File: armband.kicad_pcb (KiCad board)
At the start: 6 copper layers, 50 x 50 mm, 164 parts, among them IC1 STM32MP157AAB3, IC2 MT41K256M16TW-107_P, IC6 STPMIC1BPQR, IC7 S40FC004C1B2C00000, IC9 NXS0506UPZ, J4 Conn_01x03, SW1 SW_MEC_5G, SW2 SW_MEC_5G, U2 IS25LP064A-JLLE

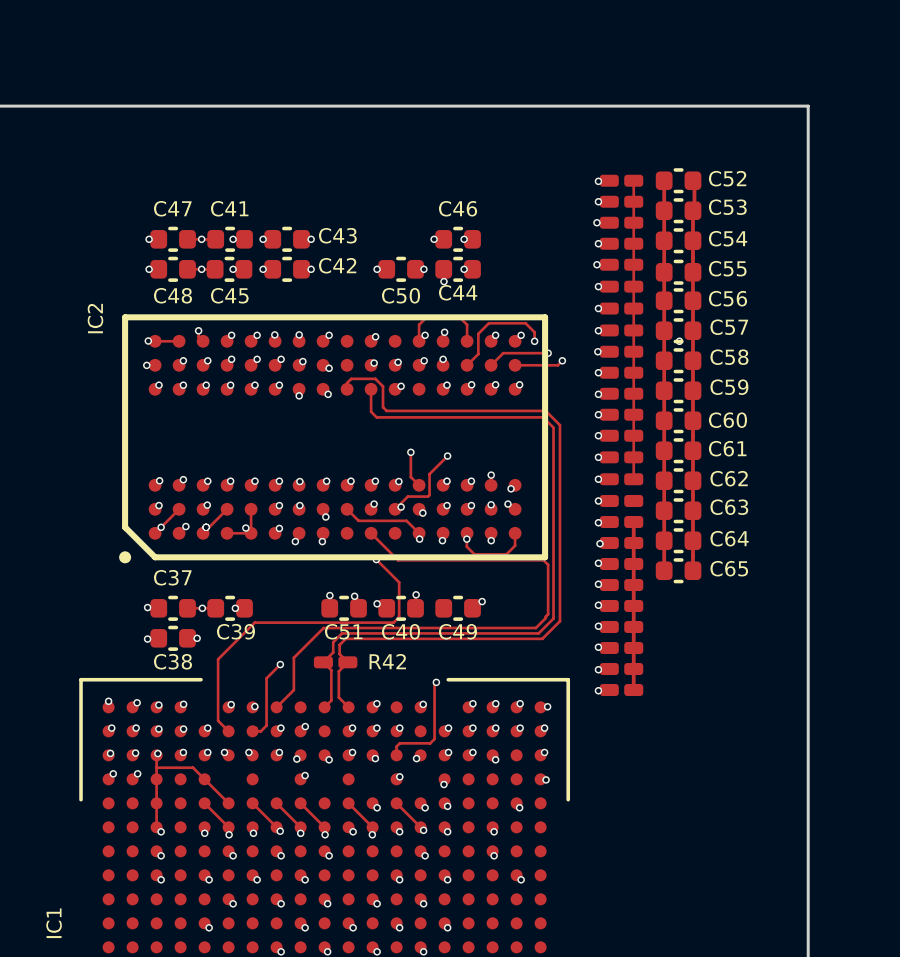
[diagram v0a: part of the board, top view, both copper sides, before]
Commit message: Add termination resistor conenctions + via for DQ
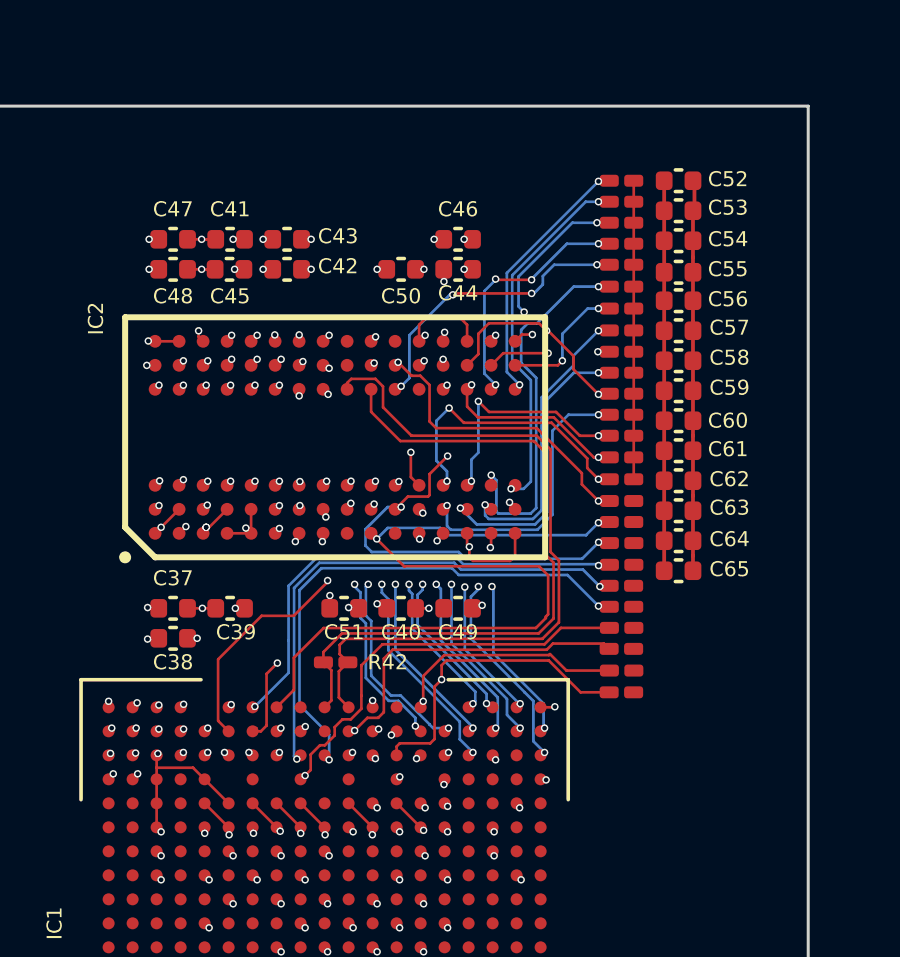
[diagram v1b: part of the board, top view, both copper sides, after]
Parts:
- moved R43 4.17 mm to (191.9, 76.7)
- moved R49 3.55 mm to (191.9, 80.2)
- moved R50 1.43 mm to (191.9, 77.3)
- moved R48 1.40 mm to (191.9, 75.9)
- moved R44 0.78 mm to (191.9, 80.9)
- moved R46 0.73 mm to (191.9, 79.5)
- moved R45 0.67 mm to (191.9, 78.8)
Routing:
- net DDR_CASN: track 24.7 -> 41.9 mm
- net DDR_WEN: track 23.2 -> 40.1 mm
- net DDR_BA0: track 18.5 -> 34.1 mm
- net DDR_BA2: track 24.1 -> 37.5 mm, vias 3 -> 2
- net DDR_A9: track 20.2 -> 32.2 mm
- net DDR_A13: track 19.1 -> 30.9 mm
- net DDR_RASN: track 24.2 -> 35.0 mm, vias 3 -> 2
- net DDR_CSN: track 22.4 -> 32.9 mm
- net DDR_A7: track 19.5 -> 29.0 mm
- net DDR_A0: track 20.5 -> 29.7 mm, vias 3 -> 4
- net DDR_A5: track 23.3 -> 32.5 mm
- net DDR_A3: track 20.3 -> 29.3 mm
- net DDR_A10: track 20.7 -> 29.6 mm, vias 3 -> 5
- net DDR_A14: track 17.2 -> 25.7 mm
- net DDR_A12: track 22.4 -> 30.7 mm, vias 3 -> 4
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
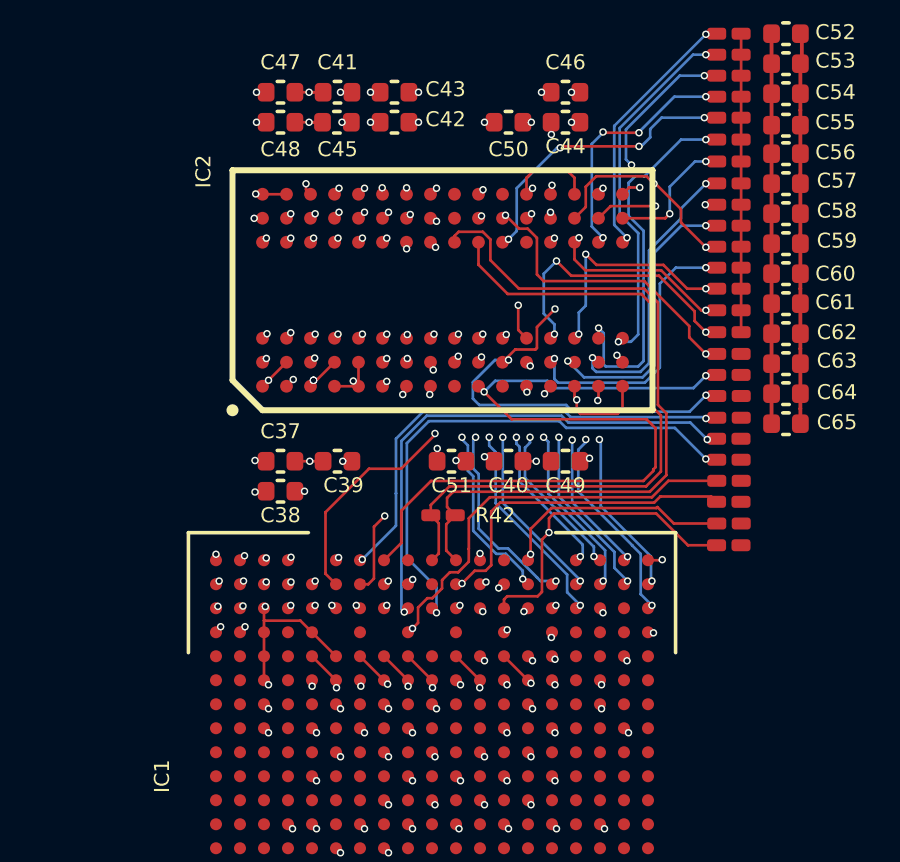
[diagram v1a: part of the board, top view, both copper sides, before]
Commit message: routed datalines - gl lengthmatching that!
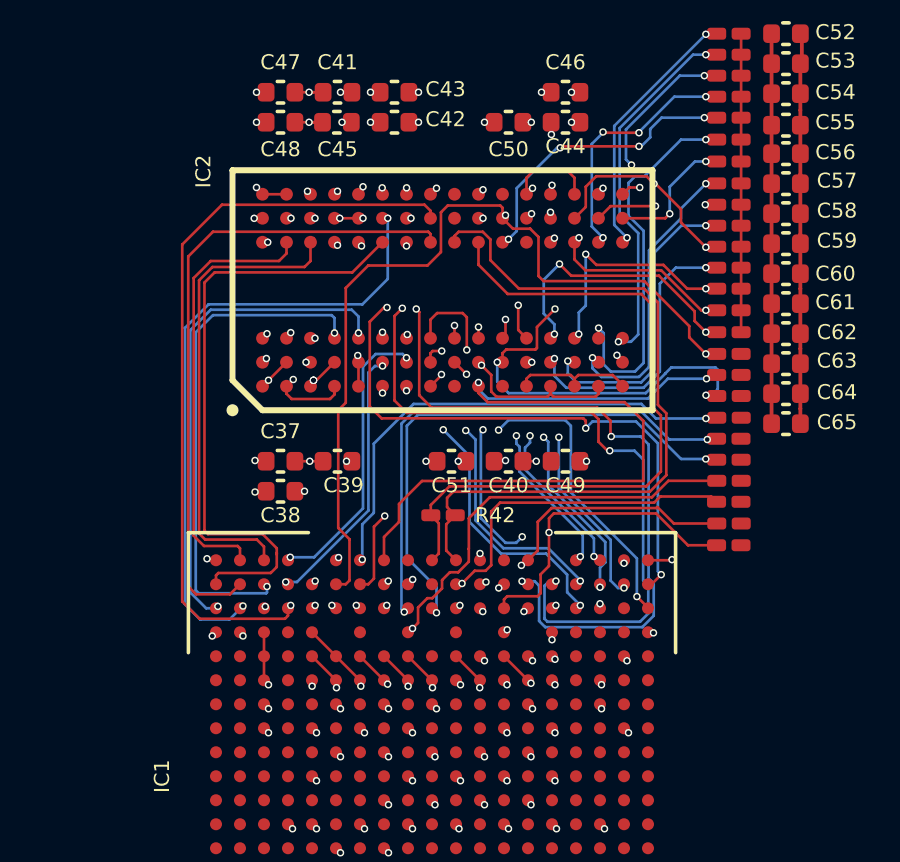
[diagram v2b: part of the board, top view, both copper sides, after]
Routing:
- net DDR_DQ5: track 0.37 -> 25.3 mm, vias 2 -> 1
- net DDR_DQ10: track 6.85 -> 29.1 mm, vias 3 -> 4
- net DDR_DQ8: track 6.20 -> 27.7 mm, vias 3 -> 4
- net DDR_DQ7: track 0.40 -> 21.7 mm, vias 2 -> 0
- net DDR_DQ3: track 0.41 -> 21.5 mm
- net DDR_DQ1: track 0.35 -> 20.7 mm, vias 2 -> 0
- net DDR_DQ12: track 5.81 -> 24.9 mm, vias 3 -> 4
- net DDR_DQM0: track 0.58 -> 16.9 mm
- net DDR_DQ0: track 0.33 -> 16.6 mm
- net DDR_DQS0_P: track 0.29 -> 16.2 mm, vias 2 -> 0
- net DDR_DQ14: track 6.11 -> 21.5 mm
- net DDR_DQ15: track 7.04 -> 21.7 mm
- net DDR_DQS0_N: track 0.41 -> 14.5 mm, vias 2 -> 0
- net DDR_DQ11: track 5.18 -> 16.8 mm, vias 3 -> 4
- net DDR_DQM1: track 6.15 -> 17.5 mm
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
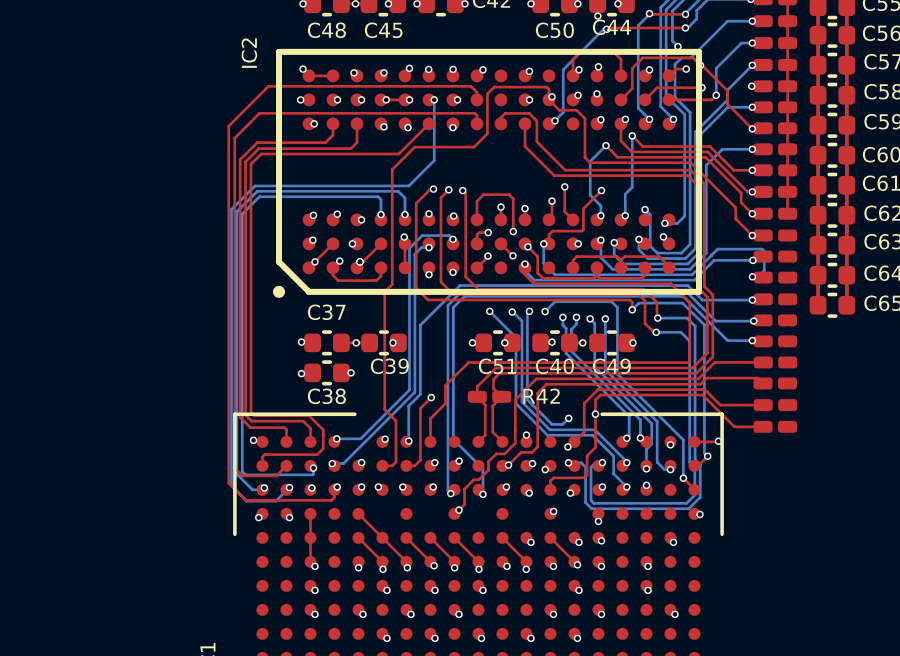
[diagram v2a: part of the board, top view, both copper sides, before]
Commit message: preperation for lengthmatching (probably 24.5mm +- 0.635)
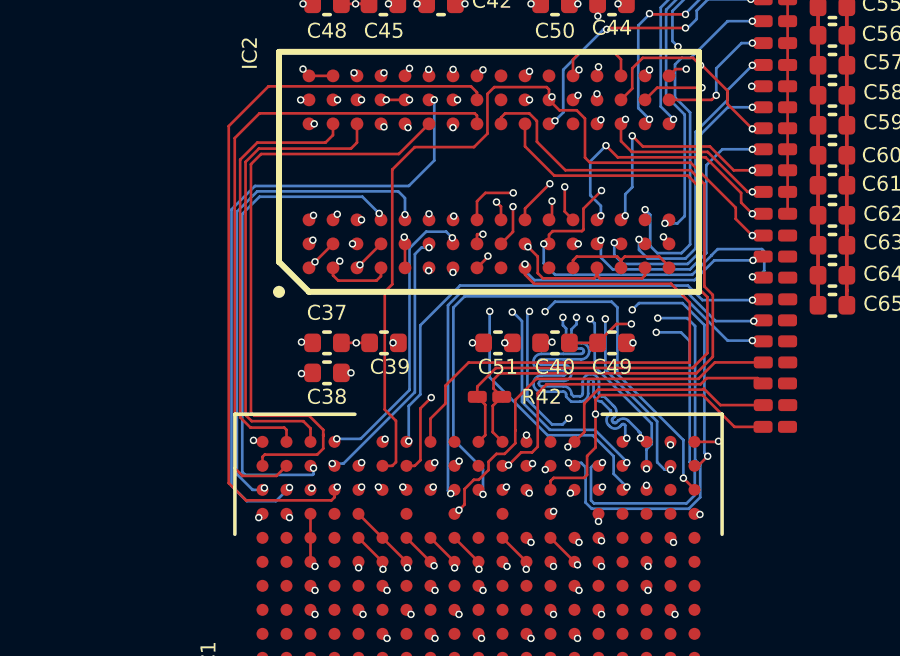
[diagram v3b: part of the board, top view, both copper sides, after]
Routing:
- net DDR_DQSI_N: track 12.0 -> 21.5 mm
- net DDR_DQSI_P: track 13.8 -> 23.3 mm
- net GND: track 76.1 -> 78.8 mm
- net DDR_DQ4: track 25.4 -> 23.5 mm
- net BUCK2_1V35: track 125.0 -> 123.2 mm, vias 37 -> 36
- net DDR_DQ15: track 21.7 -> 20.8 mm
- net DDR_DQ12: track 24.9 -> 24.0 mm, vias 4 -> 3
- net DDR_DQM1: track 17.5 -> 16.7 mm
- net DDR_DQ10: track 29.1 -> 28.6 mm, vias 4 -> 3
- net DDR_DQ8: vias 4 -> 3

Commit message: progressed length matching
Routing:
- net DDR_BA0: track 34.2 -> 40.8 mm
- net DDR_DQ9: track 15.1 -> 21.6 mm
- net DDR_ZQ: track 28.4 -> 34.8 mm
- net DDR_A13: track 30.9 -> 36.4 mm
- net DDR_DQ13: track 16.3 -> 21.5 mm
- net DDR_A7: track 29.2 -> 34.3 mm
- net DDR_DQ11: track 16.6 -> 21.6 mm
- net DDR_DQM1: track 16.7 -> 21.6 mm
- net DDR_A3: track 29.6 -> 34.5 mm
- net DDR_A0: track 29.5 -> 33.8 mm
- net DDR_A9: track 32.4 -> 36.5 mm
- net DDR_A2: track 27.6 -> 31.7 mm
- net DDR_A10: track 29.6 -> 33.6 mm
- net DDR_A11: track 25.8 -> 29.7 mm
- net DDR_A1: track 27.3 -> 29.0 mm
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
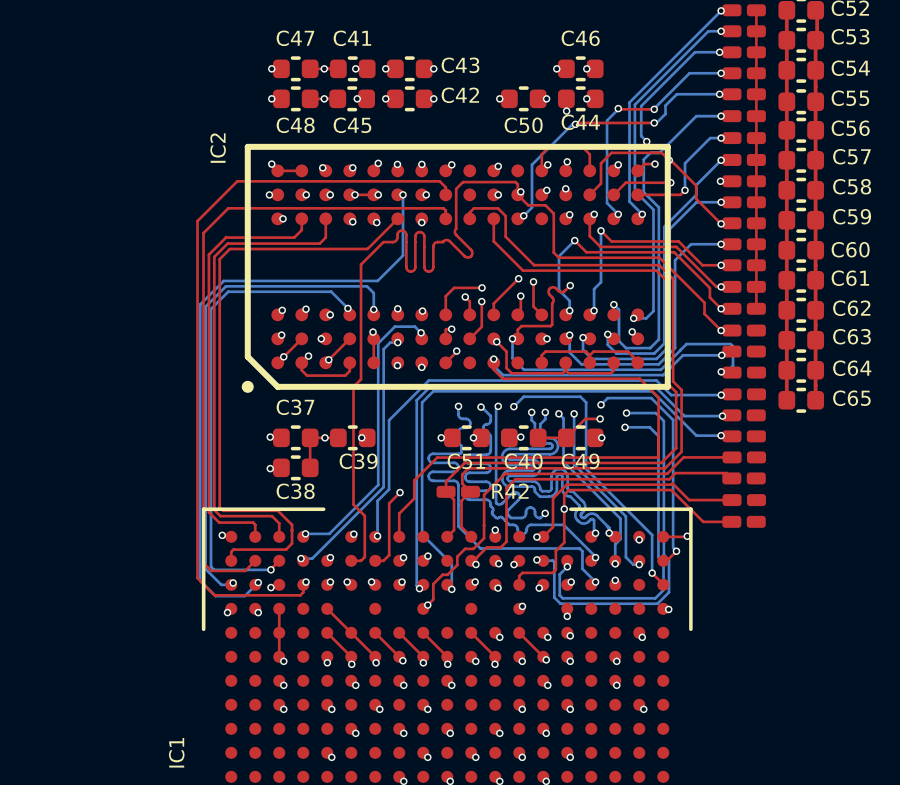
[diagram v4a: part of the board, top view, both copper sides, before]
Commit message: lengthmatched ddr traces to 24.5mm +-0.625mm
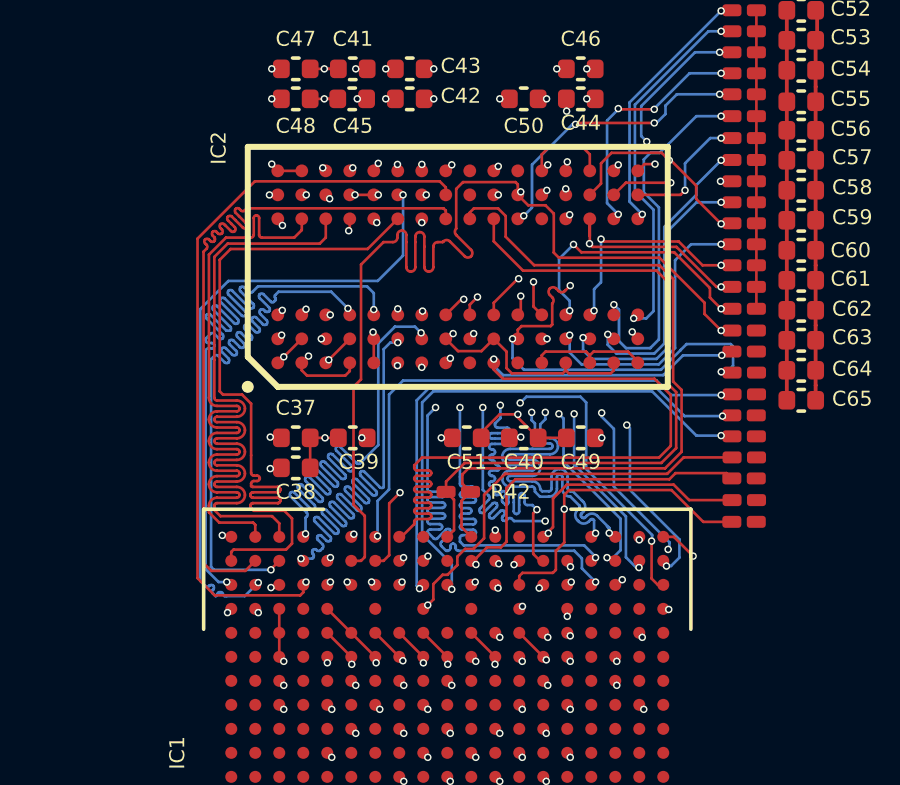
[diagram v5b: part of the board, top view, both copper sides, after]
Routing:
- net DDR_DQ2: track 9.48 -> 21.7 mm
- net DDR_DQ6: track 10.3 -> 21.8 mm
- net DDR_DQS0_N: track 14.5 -> 24.3 mm
- net DDR_DQS0_P: track 16.2 -> 24.7 mm
- net DDR_DQ0: track 16.6 -> 24.6 mm
- net DDR_A8: track 21.2 -> 28.2 mm
- net DDR_A14: track 25.7 -> 32.7 mm
- net DDR_BA1: track 27.5 -> 34.3 mm
- net DDR_DQ8: track 27.7 -> 21.5 mm
- net DDR_DQ10: track 28.2 -> 22.0 mm, vias 3 -> 4
- net DDR_ODT: track 27.4 -> 33.2 mm
- net DDR_A4: track 25.7 -> 31.1 mm
- net DDR_DQM0: track 16.3 -> 21.3 mm
- net DDR_A6: track 23.3 -> 28.2 mm
- net DDR_DQ1: track 20.7 -> 24.6 mm
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
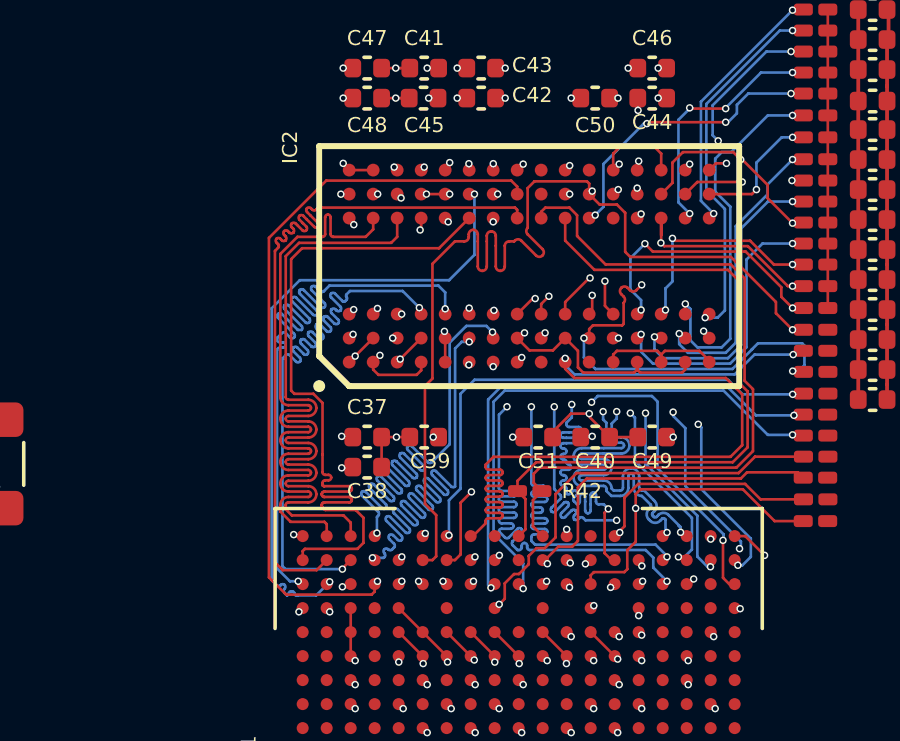
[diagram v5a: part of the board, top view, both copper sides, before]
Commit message: lengthmatching finalized
clk_p, clk_n also matched to 24.5mm
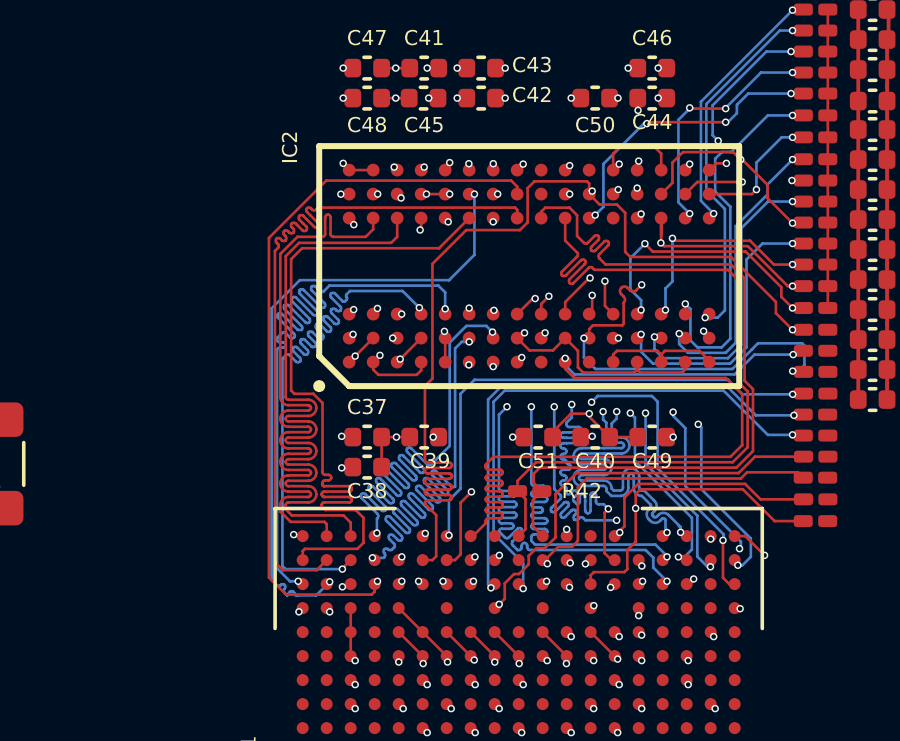
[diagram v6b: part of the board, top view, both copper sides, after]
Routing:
- net DDR_CLK_N: track 23.1 -> 26.3 mm
- net DDR_A12: track 31.0 -> 33.0 mm
- net DDR_CLK_P: track 24.4 -> 26.3 mm
